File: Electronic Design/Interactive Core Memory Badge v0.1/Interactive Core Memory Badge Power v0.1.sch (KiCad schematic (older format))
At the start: 0 parts

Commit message: Schematic Complete
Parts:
- added F1: Polyfuse, Fuse:Fuse_0805_2012Metric, symbol Device:Polyfuse
- added Q21: MMBT4401LT1G, Digikey:SOT-23-3, symbol Digikey-Transistors:MMBT4401LT1G
- added R27: 220, Resistor_SMD:R_0805_2012Metric, symbol Device:R
- added SW1: SW_SPST, Digikey:Switch_Slide_JS202011SCQN, symbol Switch:SW_SPST
- added U1: Micro_LiPo_Charger, Core_Memory_8x8_Array:Micro_LiPo_Charger, symbol CORE_64_LIBRARY:Micro_LiPo_Charger
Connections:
- net +BATT: now also SW1.1 (A), U1.4 (Bat_V+)
- net -BATT: now also Q21.2 (E), U1.2 (GND), U1.3 (BAT_GND)
- new net: F1.2, SW1.2 (B)
- new net: Q21.1 (B), R27.1
- new net +VSW: F1.1
- new net GNDPWR: Q21.3 (C)
- new net V+USB: U1.1 (5V)
- new net WRITE_ENABLE: R27.2
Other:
- note added: "Adafruit LiPo Charger Module\nHas built-in connection to battery 1S Lipo\nApprox. 3-4V operating voltage supplied to WHOLE SYSTEM."
- note added: "CORE POWER GROUND"
- note added: "Core Memory Power"
- note added: "DIGITAL LOGIC GROUND"
- note added: "IN: +BATT (3.7/4.2V) Battery is switched and fused\nOUT: +VSW\n"
- note added: "IN: +VSW\nOUT: VMEM to cores controlled by WRITE_ENABLE"
- note added: "IN: From computer USB 5V into Teensy LC module board (jumper cut to MCU onboard),\nOUT: V+USB and -BATT."
- note added: "IN: V+USB (5V) into Micro LiPo Charger circuit to charge 1S battery\nOUT: as +BATT and to onboard connector 1S battery"
- note added: "MCU, LED Array, I2C"
- note added: "POWER FLOW:"
- note added: "STAR GROUND EVERYTHING TO -BATT"
- note added: "USB V+ pad to charger module to charge from USB.\nSystem is only powered from the LiPo.\nLiPo must be connected to run."

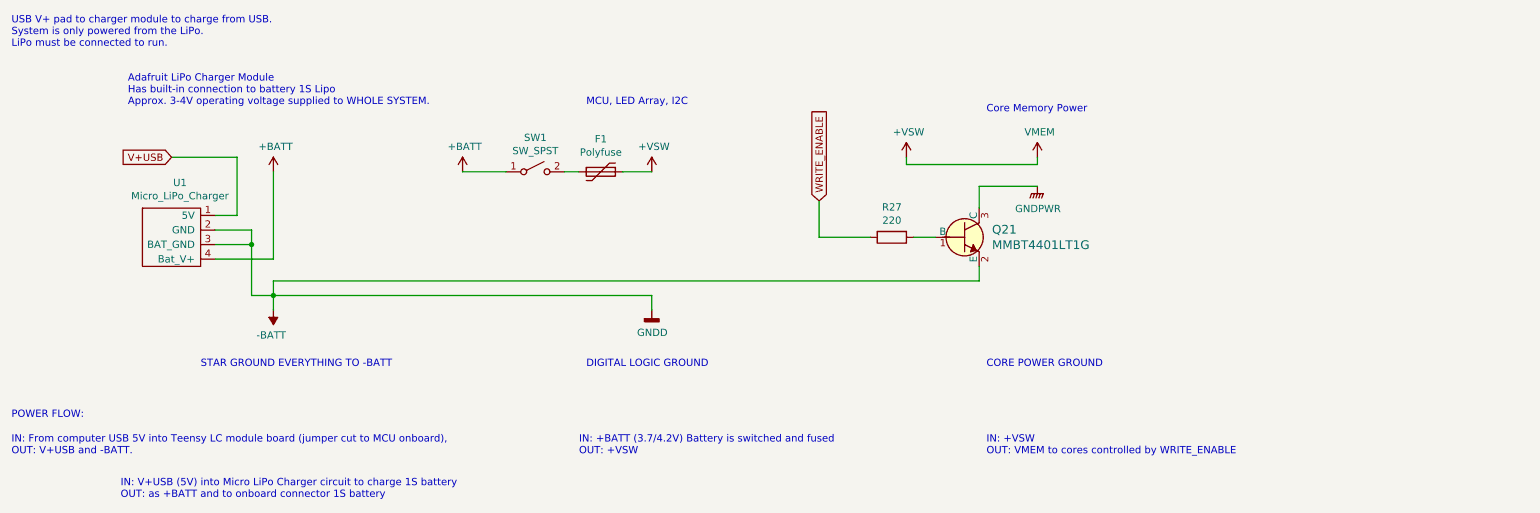
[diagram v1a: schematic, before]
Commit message: Layout 75% complete for V0.1
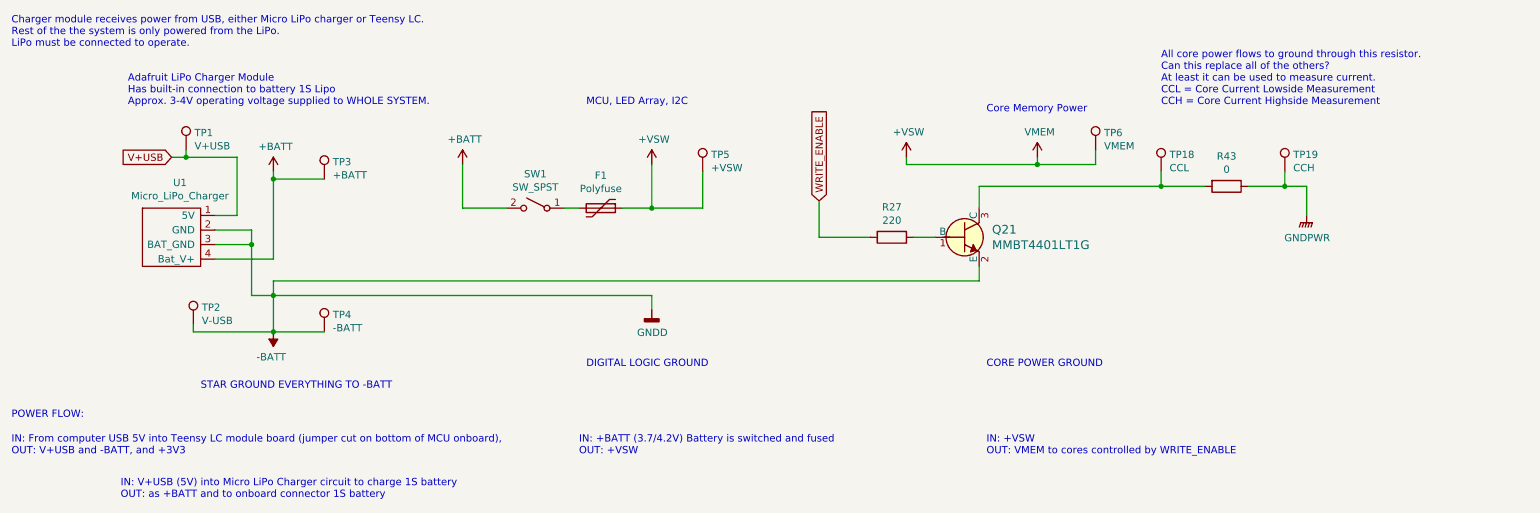
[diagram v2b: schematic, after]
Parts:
- added R43: 0, Resistor_SMD:R_0805_2012Metric, symbol Device:R
- added TP1: V+USB, TestPoint:TestPoint_Keystone_5000-5004_Miniature, symbol Connector:TestPoint
- added TP18: CCL, TestPoint:TestPoint_Keystone_5000-5004_Miniature, symbol Connector:TestPoint
- added TP19: CCH, TestPoint:TestPoint_Keystone_5000-5004_Miniature, symbol Connector:TestPoint
- added TP2: V-USB, TestPoint:TestPoint_Keystone_5000-5004_Miniature, symbol Connector:TestPoint
- added TP3: +BATT, TestPoint:TestPoint_Keystone_5000-5004_Miniature, symbol Connector:TestPoint
- added TP4: -BATT, TestPoint:TestPoint_Keystone_5000-5004_Miniature, symbol Connector:TestPoint
- added TP5: +VSW, TestPoint:TestPoint_Keystone_5000-5004_Miniature, symbol Connector:TestPoint
- added TP6: VMEM, TestPoint:TestPoint_Keystone_5000-5004_Miniature, symbol Connector:TestPoint
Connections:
- net +BATT: now also SW1.2 (B), TP3.1; no longer SW1.1 (A)
- net +VSW: now also TP5.1, TP6.1
- net -BATT: now also TP2.1, TP4.1
- net GNDPWR: now also R43.1, TP19.1; no longer Q21.3 (C)
- net V+USB: now also TP1.1
- net at F1.2: now also SW1.1 (A); no longer SW1.2 (B)
- new net: Q21.3 (C), R43.2, TP18.1
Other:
- note added: "All core power flows to ground through this resistor.\nCan this replace all of the others?\nAt least it can be used to measure current.\nCCL = Core Current Lowside Measurement\nCCH = Core Current Highside Measurement"
- note added: "Charger module receives power from USB, either Micro LiPo charger or Teensy LC.\nRest of the the system is only powered from the LiPo.\nLiPo must be connected to operate."
- note added: "IN: From computer USB 5V into Teensy LC module board (jumper cut on bottom of MCU onboard),\nOUT: V+USB and -BATT, and +3V3"
- note removed: "IN: From computer USB 5V into Teensy LC module board (jumper cut to MCU onboard),\nOUT: V+USB and -BATT."
- note removed: "USB V+ pad to charger module to charge from USB.\nSystem is only powered from the LiPo.\nLiPo must be connected to run."
- moved on the sheet: F1, SW1
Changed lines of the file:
@@
 L power:+BATT #PWR023
 U 1 1 5D2956F9
-P 3700 1700
-F 0 "#PWR023" H 3700 1550 50  0001 C CNN
-F 1 "+BATT" H 3715 1873 50  0000 C CNN
-F 2 "" H 3700 1700 50  0001 C CNN
-F 3 "" H 3700 1700 50  0001 C CNN
-	1    3700 1700
+P 3700 1650
+F 0 "#PWR023" H 3700 1500 50  0001 C CNN
+F 1 "+BATT" H 3715 1823 50  0000 C CNN
+F 2 "" H 3700 1650 50  0001 C CNN
+F 3 "" H 3700 1650 50  0001 C CNN
+	1    3700 1650
 	1    0    0    -1
 $EndComp
@@
 L Device:Polyfuse F1
 U 1 1 5D3009B0
-P 4650 1700
-F 0 "F1" V 4425 1700 50  0000 C CNN
-F 1 "Polyfuse" V 4516 1700 50  0000 C CNN
-F 2 "Fuse:Fuse_0805_2012Metric" H 4700 1500 50  0001 L CNN
-F 3 "~" H 4650 1700 50  0001 C CNN
-	1    4650 1700
+P 4650 1950
+F 0 "F1" V 4425 1950 50  0000 C CNN
+F 1 "Polyfuse" V 4516 1950 50  0000 C CNN
+F 2 "Fuse:Fuse_0805_2012Metric" H 4700 1750 50  0001 L CNN
+F 3 "~" H 4650 1950 50  0001 C CNN
+	1    4650 1950
 	0    1    1    0
 $EndComp
@@
 L Switch:SW_SPST SW1
 U 1 1 5D30313B
-P 4200 1700
-F 0 "SW1" H 4200 1935 50  0000 C CNN
-F 1 "SW_SPST" H 4200 1844 50  0000 C CNN
-F 2 "Digikey:Switch_Slide_JS202011SCQN" H 4200 1700 50  0001 C CNN
-F 3 "~" H 4200 1700 50  0001 C CNN
-	1    4200 1700
-	1    0    0    -1
-$EndComp
-Wire Wire Line
-	4400 1700 4500 1700
+P 4200 1950
+F 0 "SW1" H 4200 2185 50  0000 C CNN
+F 1 "SW_SPST" H 4200 2094 50  0000 C CNN
+F 2 "Digikey:Switch_Slide_JS202011SCQN" H 4200 1950 50  0001 C CNN
+F 3 "~" H 4200 1950 50  0001 C CNN
+	1    4200 1950
+	-1   0    0    -1
+$EndComp
+Wire Wire Line
+	4400 1950 4500 1950
 $Comp
 L power:+VSW #PWR024
 U 1 1 5D305A98
-P 5000 1700
-F 0 "#PWR024" H 5000 1550 50  0001 C CNN
-F 1 "+VSW" H 5015 1873 50  0000 C CNN
-F 2 "" H 5000 1700 50  0001 C CNN
-F 3 "" H 5000 1700 50  0001 C CNN
-	1    5000 1700
+P 5000 1650
+F 0 "#PWR024" H 5000 1500 50  0001 C CNN
+F 1 "+VSW" H 5015 1823 50  0000 C CNN
+F 2 "" H 5000 1650 50  0001 C CNN
+F 3 "" H 5000 1650 50  0001 C CNN
+	1    5000 1650
 	1    0    0    -1
 $EndComp
@@
 Adafruit LiPo Charger Module\nHas built-in connection to battery 1S Lipo\nApprox. 3-4V operating voltage supplied to WHOLE SYSTEM.
 Wire Wire Line
-	3700 1700 4000 1700
-Wire Wire Line
-	4800 1700 5000 1700
+	3700 1950 4000 1950
+Wire Wire Line
+	4800 1950 5000 1950
 Text Notes 600  850  0    50   ~ 0
-USB V+ pad to charger module to charge from USB.\nSystem is only powered from the LiPo.\nLiPo must be connected to run.
+Charger module receives power from USB, either Micro LiPo charger or Teensy LC.\nRest of the the system is only powered from the LiPo.\nLiPo must be connected to operate.
 Text GLabel 1700 1600 0    50   Input ~ 0
 V+USB
@@
 L power:-BATT #PWR022
 U 1 1 5D30A5B6
-P 2400 2650
-F 0 "#PWR022" H 2400 2500 50  0001 C CNN
-F 1 "-BATT" H 2415 2823 50  0000 C CNN
-F 2 "" H 2400 2650 50  0001 C CNN
-F 3 "" H 2400 2650 50  0001 C CNN
-	1    2400 2650
+P 2400 2800
+F 0 "#PWR022" H 2400 2650 50  0001 C CNN
+F 1 "-BATT" H 2415 2973 50  0000 C CNN
+F 2 "" H 2400 2800 50  0001 C CNN
+F 3 "" H 2400 2800 50  0001 C CNN
+	1    2400 2800
 	-1   0    0    1
 $EndComp
@@
 	2000 2300 2400 2300
 Wire Wire Line
-	2400 2300 2400 1700
-Text Notes 1900 3050 0    50   ~ 0
+	2400 2300 2400 1750
+Text Notes 1900 3200 0    50   ~ 0
 STAR GROUND EVERYTHING TO -BATT
 Text GLabel 6150 1900 1    50   Input ~ 0
@@
 POWER FLOW:
 Text Notes 600  3650 0    50   ~ 0
-IN: From computer USB 5V into Teensy LC module board (jumper cut to MCU onboard),\nOUT: V+USB and -BATT.
+IN: From computer USB 5V into Teensy LC module board (jumper cut on bottom of MCU onboard),\nOUT: V+USB and -BATT, and +3V3
 Text Notes 7300 3650 0    50   ~ 0
 IN: +VSW\nOUT: VMEM to cores controlled by WRITE_ENABLE
@@
 	2250 2550 2400 2550
 Wire Wire Line
-	2400 2550 2400 2650
-Wire Wire Line
-	1700 1600 2150 1600
+	2400 2550 2400 2800
+Wire Wire Line
+	1700 1600 1800 1600
 Wire Wire Line
 	2150 2000 2150 1600
@@
 L power:GNDPWR #PWR?
 U 1 1 5D35C3D6
-P 7650 1800
+P 9500 2000
 AR Path="/5D35C3D6" Ref="#PWR?"  Part="1"
 AR Path="/5D254AE8/5D35C3D6" Ref="#PWR028"  Part="1"
-F 0 "#PWR028" H 7650 1600 50  0001 C CNN
-F 1 "GNDPWR" H 7654 1646 50  0000 C CNN
-F 2 "" H 7650 1750 50  0001 C CNN
-F 3 "" H 7650 1750 50  0001 C CNN
-	1    7650 1800
-	1    0    0    -1
-$EndComp
-Wire Wire Line
-	7250 1800 7650 1800
+F 0 "#PWR028" H 9500 1800 50  0001 C CNN
+F 1 "GNDPWR" H 9504 1846 50  0000 C CNN
+F 2 "" H 9500 1950 50  0001 C CNN
+F 3 "" H 9500 1950 50  0001 C CNN
+	1    9500 2000
+	1    0    0    -1
+$EndComp
+Wire Wire Line
+	7250 1800 8500 1800
 Wire Wire Line
 	6150 2150 6500 2150
@@
 Text Notes 4550 1250 0    50   ~ 0
 MCU, LED Array, I2C
+$Comp
+L Connector:TestPoint TP1
+U 1 1 5D48B700
+P 1800 1550
+F 0 "TP1" H 1858 1668 50  0000 L CNN
+F 1 "V+USB" H 1858 1577 50  0000 L CNN
+F 2 "TestPoint:TestPoint_Keystone_5000-5004_Miniature" H 2000 1550 50  0001 C CNN
+F 3 "~" H 2000 1550 50  0001 C CNN
+	1    1800 1550
+	1    0    0    -1
+$EndComp
+Wire Wire Line
+	1800 1550 1800 1600
+Connection ~ 1800 1600
+Wire Wire Line
+	1800 1600 2150 1600
+$Comp
+L Connector:TestPoint TP3
+U 1 1 5D48C4DD
+P 2750 1750
+F 0 "TP3" H 2808 1868 50  0000 L CNN
+F 1 "+BATT" H 2808 1777 50  0000 L CNN
+F 2 "TestPoint:TestPoint_Keystone_5000-5004_Miniature" H 2950 1750 50  0001 C CNN
+F 3 "~" H 2950 1750 50  0001 C CNN
+	1    2750 1750
+	1    0    0    -1
+$EndComp
+Wire Wire Line
+	2400 1750 2750 1750
+Connection ~ 2400 1750
+Wire Wire Line
+	2400 1750 2400 1700
+$Comp
+L Connector:TestPoint TP4
+U 1 1 5D48D068
+P 2750 2800
+F 0 "TP4" H 2808 2918 50  0000 L CNN
+F 1 "-BATT" H 2808 2827 50  0000 L CNN
+F 2 "TestPoint:TestPoint_Keystone_5000-5004_Miniature" H 2950 2800 50  0001 C CNN
+F 3 "~" H 2950 2800 50  0001 C CNN
+	1    2750 2800
+	1    0    0    -1
+$EndComp
+Wire Wire Line
+	2750 2800 2400 2800
+Connection ~ 2400 2800
+$Comp
+L Connector:TestPoint TP5
+U 1 1 5D48E646
+P 5350 1700
+F 0 "TP5" H 5408 1818 50  0000 L CNN
+F 1 "+VSW" H 5408 1727 50  0000 L CNN
+F 2 "TestPoint:TestPoint_Keystone_5000-5004_Miniature" H 5550 1700 50  0001 C CNN
+F 3 "~" H 5550 1700 50  0001 C CNN
+	1    5350 1700
+	1    0    0    -1
+$EndComp
+Wire Wire Line
+	5000 1950 5350 1950
+Wire Wire Line
+	5350 1950 5350 1700
+Connection ~ 5000 1950
+$Comp
+L Connector:TestPoint TP6
+U 1 1 5D48F2A7
+P 8050 1550
+F 0 "TP6" H 8108 1668 50  0000 L CNN
+F 1 "VMEM" H 8108 1577 50  0000 L CNN
+F 2 "TestPoint:TestPoint_Keystone_5000-5004_Miniature" H 8250 1550 50  0001 C CNN
+F 3 "~" H 8250 1550 50  0001 C CNN
+	1    8050 1550
+	1    0    0    -1
+$EndComp
+Wire Wire Line
+	7650 1650 8050 1650
+Wire Wire Line
+	8050 1650 8050 1550
+Connection ~ 7650 1650
+Wire Wire Line
+	9500 2000 9500 1800
+Wire Wire Line
+	3700 1950 3700 1650
+Wire Wire Line
+	5000 1650 5000 1950
+$Comp
+L Connector:TestPoint TP2
+U 1 1 5D542466
+P 1850 2750
+F 0 "TP2" H 1908 2868 50  0000 L CNN
+F 1 "V-USB" H 1908 2777 50  0000 L CNN
+F 2 "TestPoint:TestPoint_Keystone_5000-5004_Miniature" H 2050 2750 50  0001 C CNN
+F 3 "~" H 2050 2750 50  0001 C CNN
+	1    1850 2750
+	1    0    0    -1
+$EndComp
+Wire Wire Line
+	1850 2750 1850 2800
+Wire Wire Line
+	1850 2800 2400 2800
+$Comp
+L Device:R R?
+U 1 1 5D4B5807
+P 8950 1800
+AR Path="/5D4B5807" Ref="R?"  Part="1"
+AR Path="/5D254AE8/5D4B5807" Ref="R43"  Part="1"
+F 0 "R43" V 8743 1800 50  0000 C CNN
+F 1 "0" V 8834 1800 50  0000 C CNN
+F 2 "Resistor_SMD:R_0805_2012Metric" V 8880 1800 50  0001 C CNN
+F 3 "~" H 8950 1800 50  0001 C CNN
+	1    8950 1800
+	0    1    1    0
+$EndComp
+Wire Wire Line
+	9100 1800 9350 1800
+Text Notes 8500 1250 0    50   ~ 0
+All core power flows to ground through this resistor.\nCan this replace all of the others?\nAt least it can be used to measure current.\nCCL = Core Current Lowside Measurement\nCCH = Core Current Highside Measurement
+$Comp
+L Connector:TestPoint TP18
+U 1 1 5D4B94F7
+P 8500 1700
+F 0 "TP18" H 8558 1818 50  0000 L CNN
+F 1 "CCL" H 8558 1727 50  0000 L CNN
+F 2 "TestPoint:TestPoint_Keystone_5000-5004_Miniature" H 8700 1700 50  0001 C CNN
+F 3 "~" H 8700 1700 50  0001 C CNN
+	1    8500 1700
+	1    0    0    -1
+$EndComp
+$Comp
+L Connector:TestPoint TP19
+U 1 1 5D4B9C69
+P 9350 1700
+F 0 "TP19" H 9408 1818 50  0000 L CNN
+F 1 "CCH" H 9408 1727 50  0000 L CNN
+F 2 "TestPoint:TestPoint_Keystone_5000-5004_Miniature" H 9550 1700 50  0001 C CNN
+F 3 "~" H 9550 1700 50  0001 C CNN
+	1    9350 1700
+	1    0    0    -1
+$EndComp
+Wire Wire Line
+	9350 1700 9350 1800
+Connection ~ 9350 1800
+Wire Wire Line
+	9350 1800 9500 1800
+Wire Wire Line
+	8500 1700 8500 1800
+Connection ~ 8500 1800
+Wire Wire Line
+	8500 1800 8800 1800
 $EndSCHEMATC
